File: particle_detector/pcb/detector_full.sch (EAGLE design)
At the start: 37 parts, among them IC1 LT1807R, IC2 SENSL-SIPM, IC3 LT3461, IC4 TEENSY_3.2_NO_BOTTOM

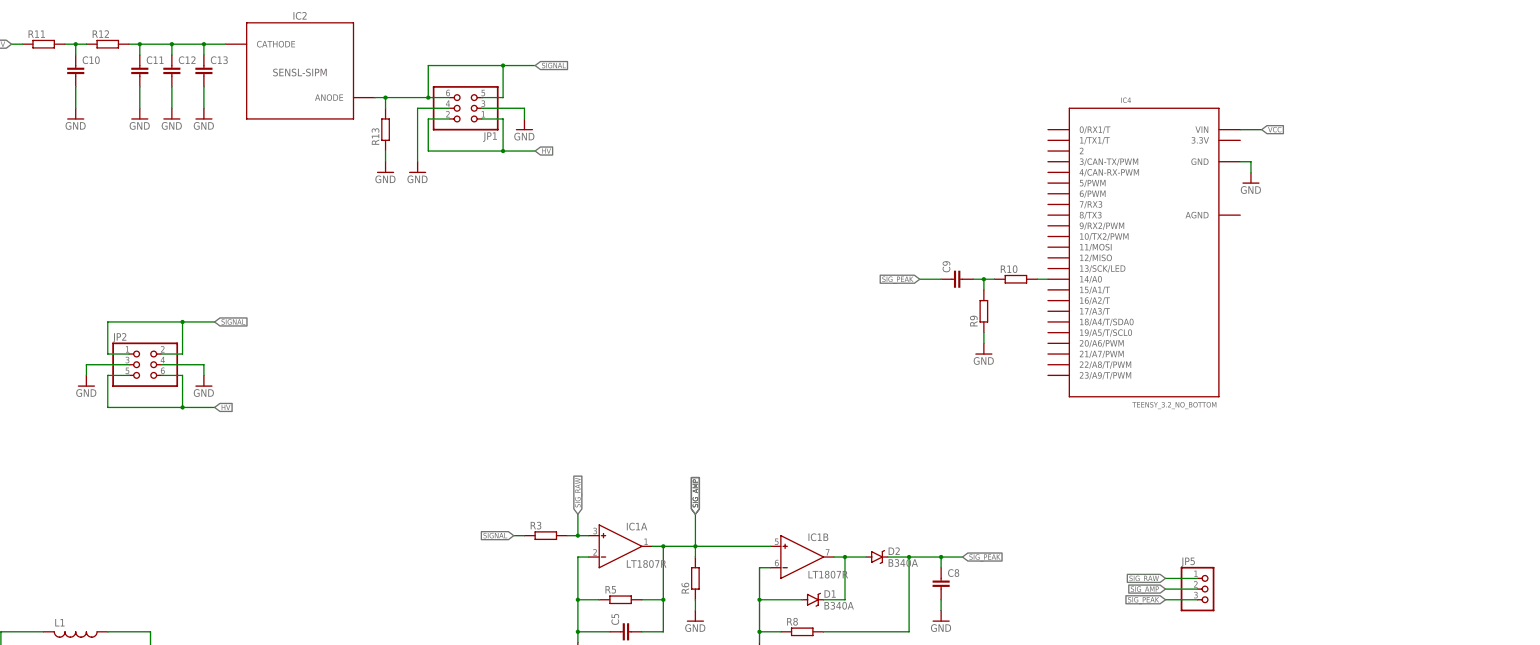
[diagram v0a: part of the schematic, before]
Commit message: change EDA name to split boards
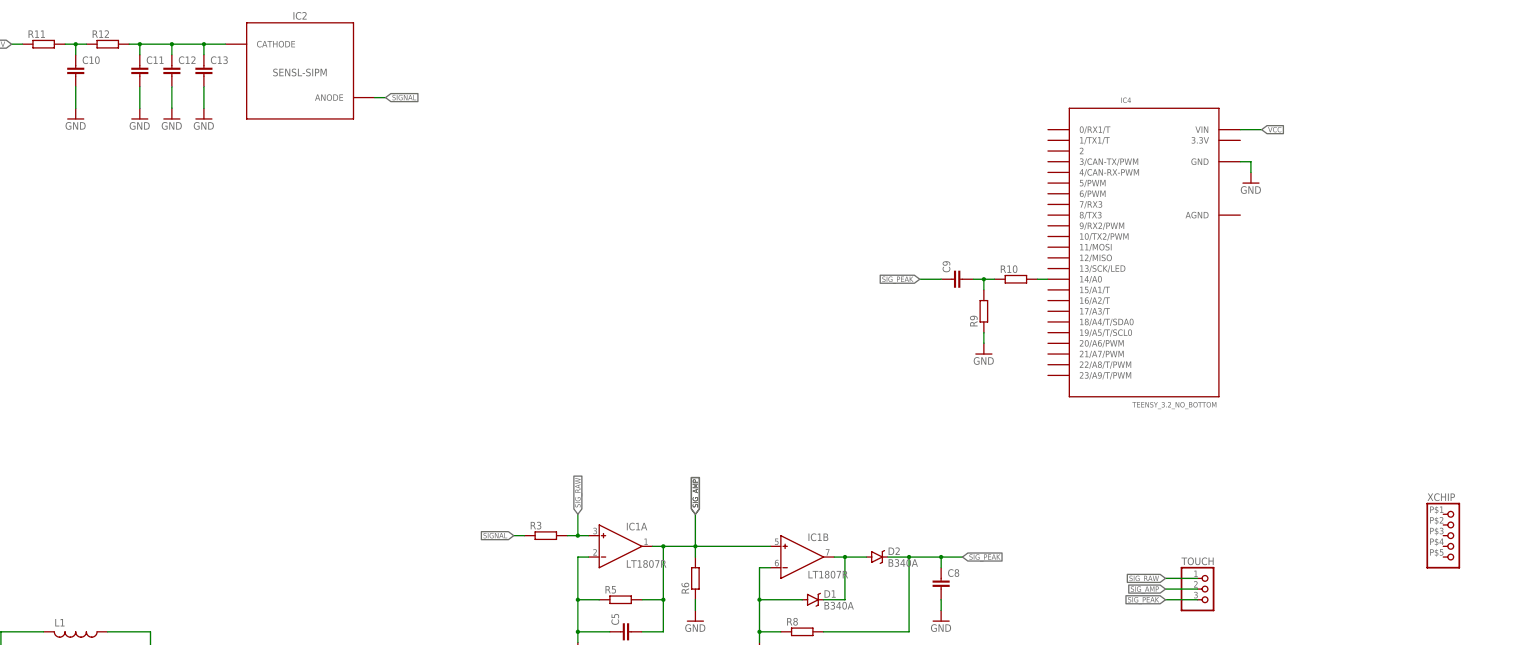
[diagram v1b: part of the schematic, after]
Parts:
- removed JP1, JP2: (no value), pinhead:PINHD-2X3
- removed R13: (no value), rcl:R-EU_M0805
- added XCHIP: (no value), personal:XCHIP-1X5
- C1, C10, C11, C12, C13, C2, C3, C4, C5, C6, C7, C8, C9: device rcl:C-EUC0805 -> rcl:C-EUC0805K
- renumbered JP5 to TOUCH
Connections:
- net GND: no longer JP1.3, JP1.4, JP2.3, JP2.4, R13.1
- net HV: no longer JP1.1, JP1.2, JP2.5, JP2.6
- net SIGNAL: no longer JP1.5, JP1.6, JP2.1, JP2.2, R13.2
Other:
- note removed: "SiPM Connection"
